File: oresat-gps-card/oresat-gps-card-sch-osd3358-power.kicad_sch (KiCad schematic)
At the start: 48 parts, among them Q6 MMBT2907, U1 OSD3358-512M-BSM, U10 SN74LVC1G07DCK, U14 TLVH431

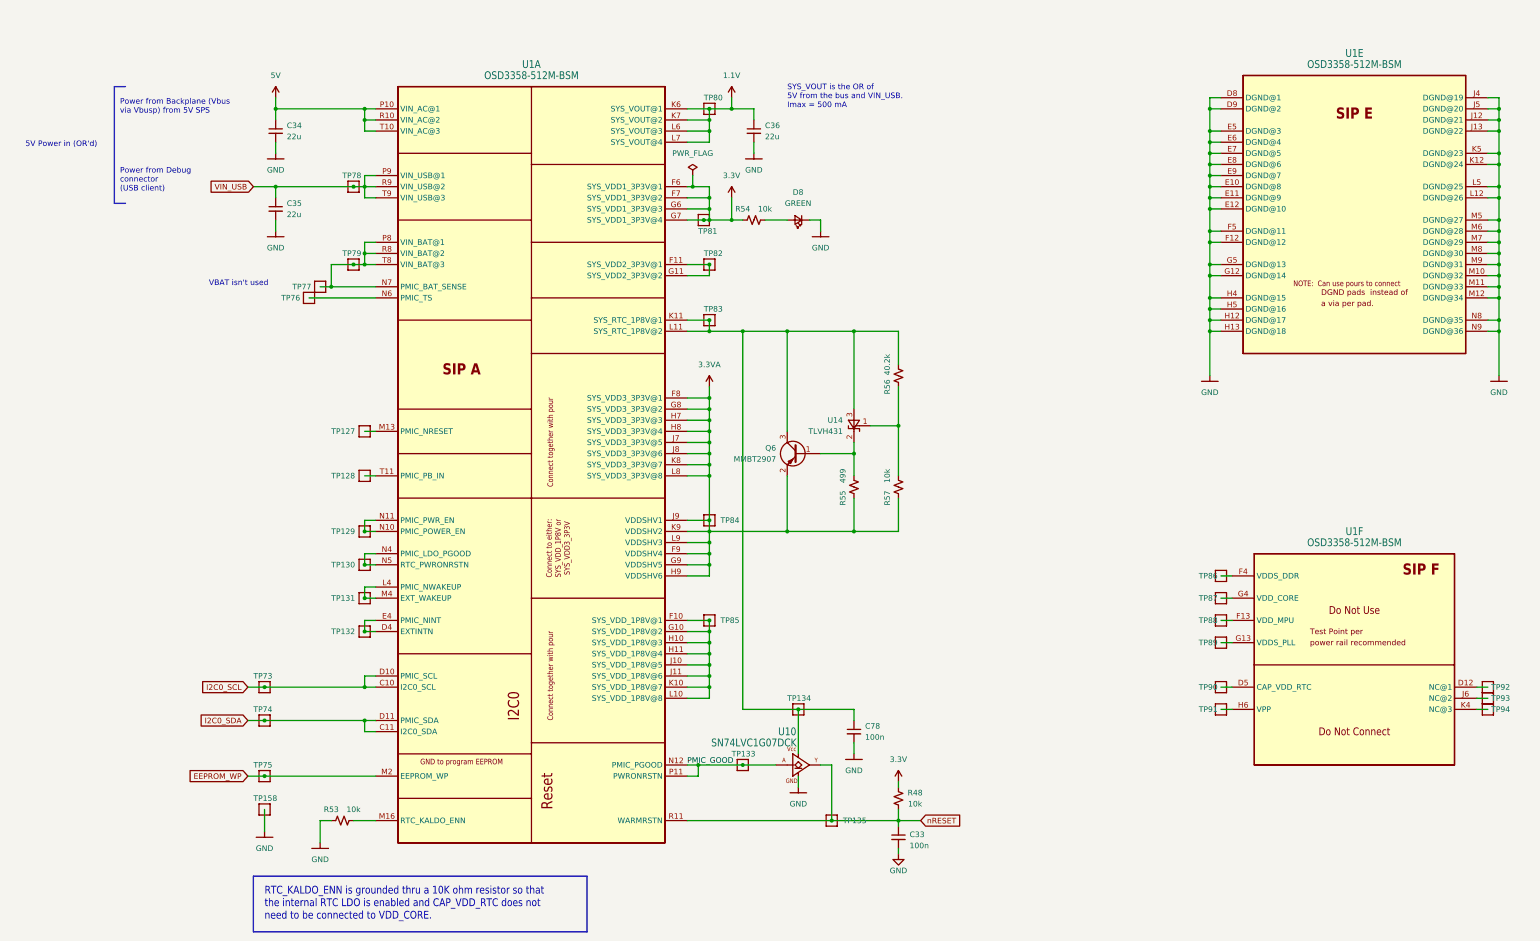
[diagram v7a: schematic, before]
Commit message: updated symbols and started new 2771 symbol
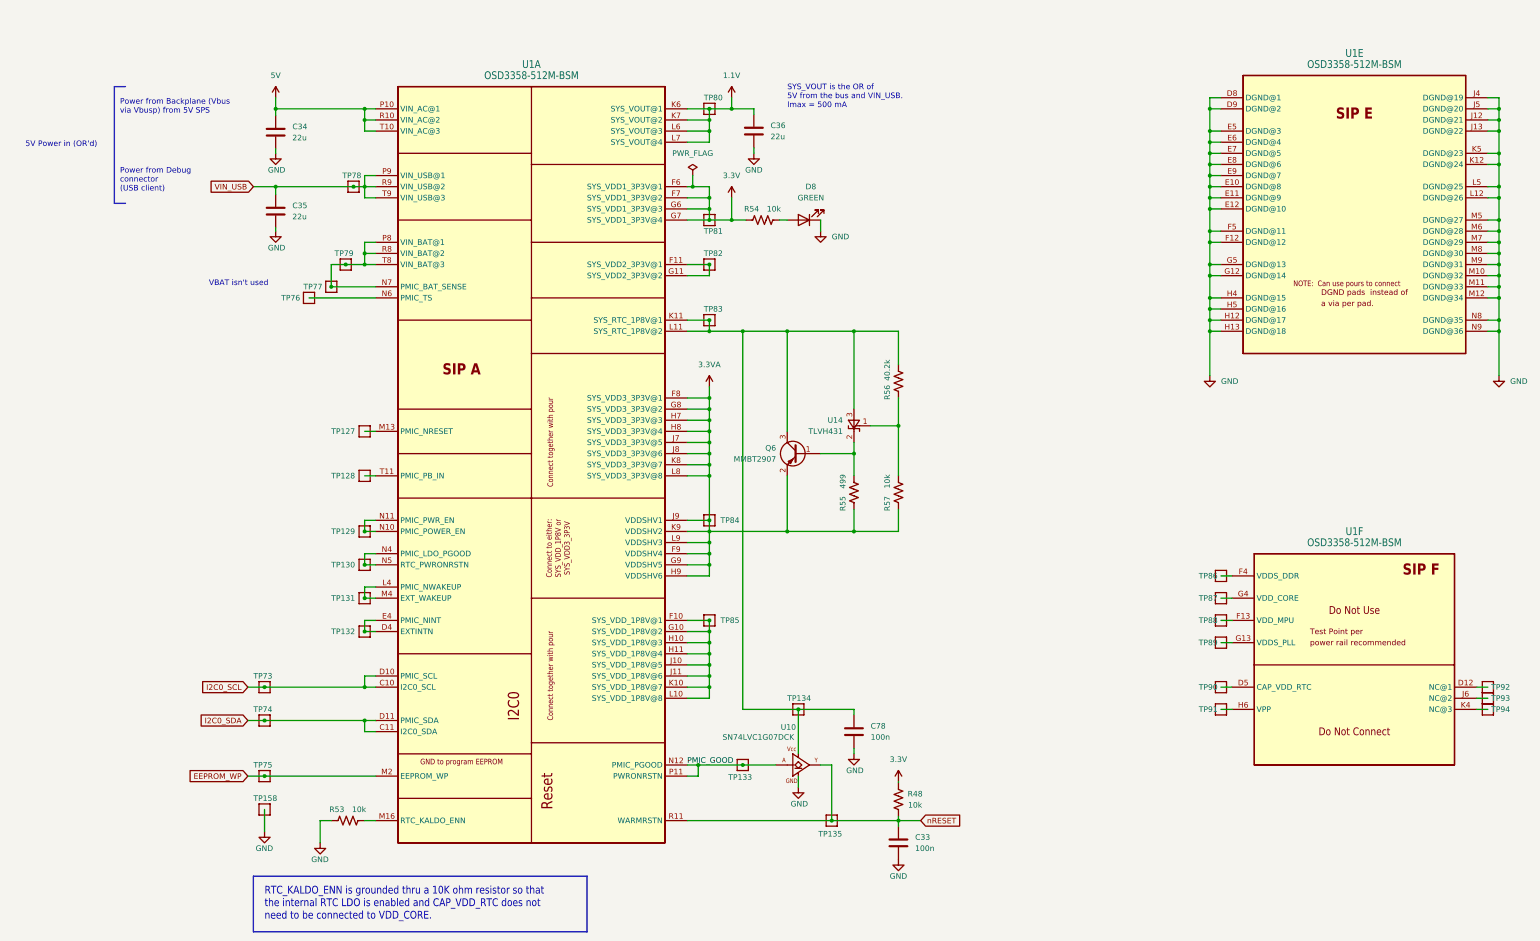
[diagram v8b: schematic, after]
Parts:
- C33, C34, C35, C36, C78: symbol Device:C_Small -> Device:C
- D8: symbol Device:LED_Small -> Device:LED
- R48, R53, R54, R55, R56, R57: symbol Device:R_Small_US -> Device:R_US
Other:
- moved on the sheet: C33, C35, D8, TP77, TP79, TP81
